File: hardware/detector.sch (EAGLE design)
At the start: 38 parts, among them J1 AVR_SPI_PRG_6NS, Q1 16MHz, T1 BC337, T2 BC337, T3 78601, U1 TINY85-20-DIP

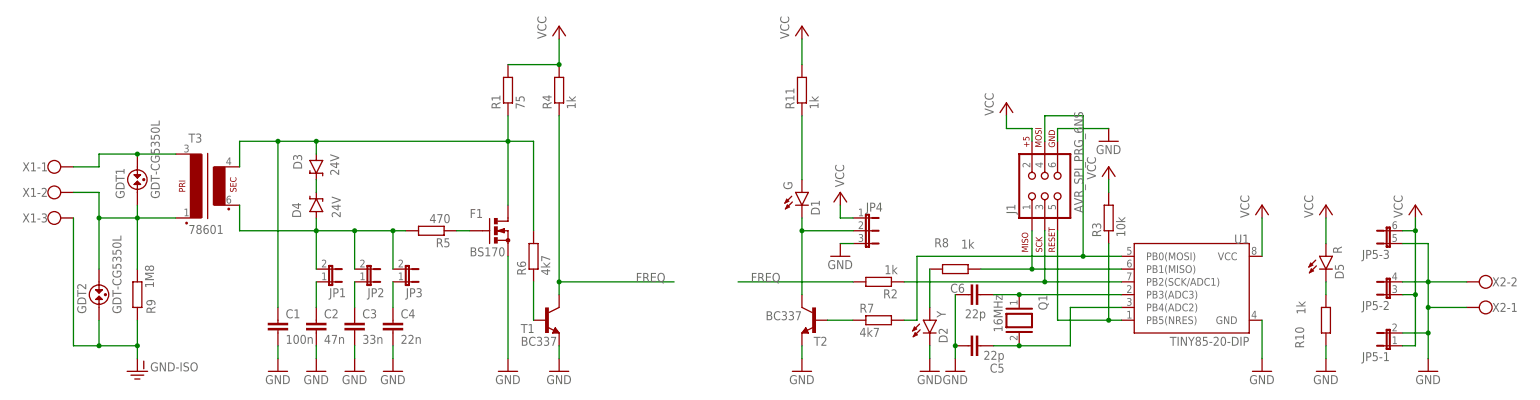
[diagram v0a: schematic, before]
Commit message: hardware: replaced impulse transformer, VCC capacitors added
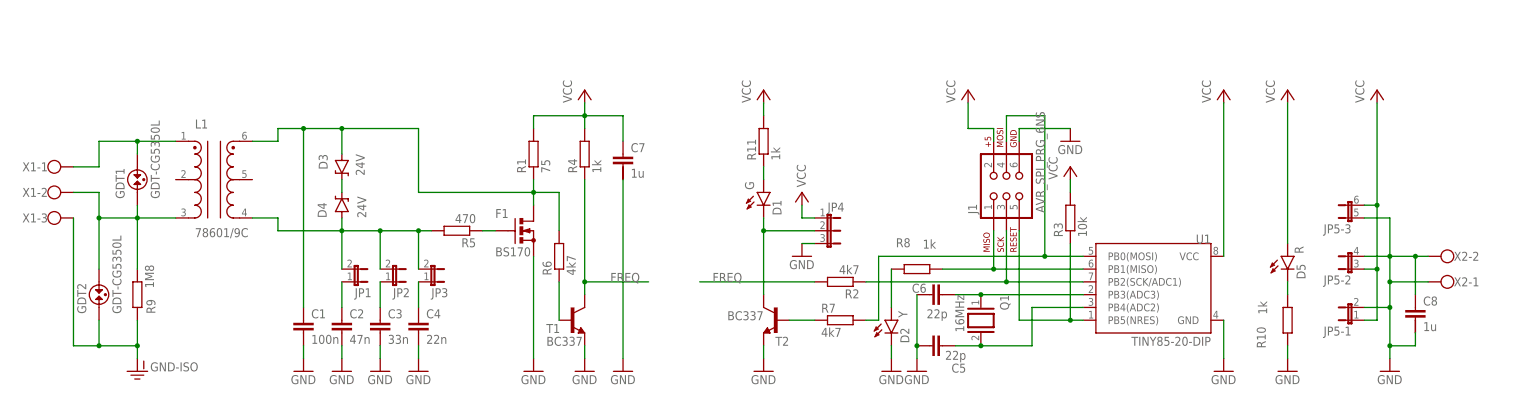
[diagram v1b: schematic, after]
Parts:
- removed T3: 78601, trafo-murata:78601
- added C7, C8: 1u, capacitor-wima:C-2.5-5/4
- added L1: 78601/9C, detector:78601/9C
- R1: device resistor:R-EU_0204/5 -> resistor:R-EU_0204/7
- R2: value 1k -> 4k7
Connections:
- removed net N$20: GDT1.2, T3.P2, X1-1.KL
- new net N$7: GDT1.2, L1.1, X1-1.KL
- net GND: now also C7.2, C8.1, C8.2
- net N$14: now also L1.6; no longer T3.S2
- net N$21: now also L1.3; no longer T3.P1
- net N$6: now also L1.4; no longer T3.S1
- net VCC: now also C7.1
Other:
- moved on the sheet: C1, C2, C3, C4, C5, C6, D1, D2, D3, D4, D5, F1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
